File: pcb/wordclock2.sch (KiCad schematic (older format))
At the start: 3 parts

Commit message: progress
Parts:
- added BT?: Battery_Cell, symbol Battery_Cell
- added C?: 100u, symbol C
- added C?: 10u, symbol C
- added C? (x3): 100n, symbol C
- added C? (x4): 22p, symbol C
- added J?: Jack-DC, symbol Jack-DC
- added J?: USB_OTG, symbol USB_OTG
- added U?: Si7021, symbol Si7021
- added U?: TPS77833_SO8, Housings_SOIC:SOIC-8_3.9x4.9mm_Pitch1.27mm, symbol TPS77833_SO8
- added Y?: 32.768kHz, symbol Crystal
- added Y?: 8MHz, symbol Crystal
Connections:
- net labels added: +3.3V, +5V, GND, USB_DM, USB_DP
- wire segments 0 -> 61
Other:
- moved on the sheet: U?

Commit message: progress
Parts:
- added BZ?: Buzzer, symbol Buzzer
- added J?: Micro_SD_Card_Det, symbol Micro_SD_Card_Det
- added J? (x2): CONN_01X03, symbol CONN_01X03
- added J?: CONN_02X05, symbol CONN_02X05
- added JP?: Jumper_NO_Small, symbol Jumper_NO_Small
- added R? (x3): 4k7, symbol R
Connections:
- net labels added: BOOT0, ST_NRST, SWCLK, SWDIO, SWO, UART_DBG_RX, UART_DBG_TX, UART_WLAN_RX, UART_WLAN_TX
- wire segments 61 -> 101

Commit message: progress
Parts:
- added Q? (x2): FDS6890A, Housings_SOIC:SOIC-8_3.9x4.9mm_Pitch1.27mm, symbol FDS6890A
- added SW?: SW_Push, symbol SW_Push
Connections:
- wire segments 101 -> 116
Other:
- moved on the sheet: BZ?, J?
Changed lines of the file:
@@
 encoding utf-8
 Sheet 1 1
-Title ""
+Title "Wordclock2"
 Date ""
 Rev ""
@@
 L Micro_SD_Card_Det J?
 U 1 1 5983AA78
-P 5150 6750
-F 0 "J?" H 4500 7450 50  0000 C CNN
-F 1 "Micro_SD_Card_Det" H 5800 7450 50  0000 R CNN
-F 2 "" H 7200 7450 50  0001 C CNN
-F 3 "" H 5150 6850 50  0001 C CNN
-	1    5150 6750
+P 5150 6500
+F 0 "J?" H 4500 7200 50  0000 C CNN
+F 1 "Micro_SD_Card_Det" H 5800 7200 50  0000 R CNN
+F 2 "" H 7200 7200 50  0001 C CNN
+F 3 "" H 5150 6600 50  0001 C CNN
+	1    5150 6500
 	1    0    0    -1
 $EndComp
@@
 L Buzzer BZ?
 U 1 1 5983AD21
-P 3800 5450
-F 0 "BZ?" H 3950 5500 50  0000 L CNN
-F 1 "Buzzer" H 3950 5400 50  0000 L CNN
-F 2 "" V 3775 5550 50  0001 C CNN
-F 3 "" V 3775 5550 50  0001 C CNN
-	1    3800 5450
+P 3750 5100
+F 0 "BZ?" H 3900 5150 50  0000 L CNN
+F 1 "Buzzer" H 3900 5050 50  0000 L CNN
+F 2 "" V 3725 5200 50  0001 C CNN
+F 3 "" V 3725 5200 50  0001 C CNN
+	1    3750 5100
 	1    0    0    -1
 $EndComp
@@
 	4600 700  4600 650
 Wire Wire Line
-	5150 900  5550 900
-Text Label 5200 900  0    60   ~ 0
+	5150 900  5800 900
+Text Label 5200 800  0    60   ~ 0
 BOOT0
 Wire Wire Line
@@
 Wire Wire Line
 	5150 800  5800 800
-Text Label 5150 800  0    60   ~ 0
+Text Label 5200 900  0    60   ~ 0
 UART_DBG_RX
 $Comp
@@
 Wire Wire Line
 	5900 1200 5900 1150
+$Comp
+L SW_Push SW?
+U 1 1 5984DFFE
+P 1300 3100
+F 0 "SW?" H 1350 3200 50  0000 L CNN
+F 1 "SW_Push" H 1300 3040 50  0000 C CNN
+F 2 "" H 1300 3300 50  0001 C CNN
+F 3 "" H 1300 3300 50  0001 C CNN
+	1    1300 3100
+	1    0    0    -1
+$EndComp
+$Comp
+L GND #PWR?
+U 1 1 5984E29E
+P 1050 3150
+F 0 "#PWR?" H 1050 2900 50  0001 C CNN
+F 1 "GND" H 1050 3000 50  0000 C CNN
+F 2 "" H 1050 3150 50  0001 C CNN
+F 3 "" H 1050 3150 50  0001 C CNN
+	1    1050 3150
+	1    0    0    -1
+$EndComp
+Wire Wire Line
+	1100 3100 1050 3100
+Wire Wire Line
+	1050 3100 1050 3150
+Wire Wire Line
+	1500 3100 1950 3100
+Text Label 1550 3100 0    60   ~ 0
+ST_NRST
+$Comp
+L FDS6890A Q?
+U 1 1 5984ED73
+P 3700 7300
+F 0 "Q?" H 3950 7375 50  0000 L CNN
+F 1 "FDS6890A" H 3950 7300 50  0000 L CNN
+F 2 "Housings_SOIC:SOIC-8_3.9x4.9mm_Pitch1.27mm" H 3950 7225 50  0001 L CIN
+F 3 "" H 3700 7300 50  0001 L CNN
+	1    3700 7300
+	1    0    0    -1
+$EndComp
+$Comp
+L FDS6890A Q?
+U 2 1 5984F828
+P 3450 5500
+F 0 "Q?" H 3700 5575 50  0000 L CNN
+F 1 "FDS6890A" H 3700 5500 50  0000 L CNN
+F 2 "Housings_SOIC:SOIC-8_3.9x4.9mm_Pitch1.27mm" H 3700 5425 50  0001 L CIN
+F 3 "" H 3450 5500 50  0001 L CNN
+	2    3450 5500
+	1    0    0    -1
+$EndComp
+Wire Wire Line
+	3650 5200 3550 5200
+Wire Wire Line
+	3550 5200 3550 5300
+Wire Wire Line
+	3650 5200 3650 5300
+Wire Wire Line
+	3550 5700 3550 5750
+$Comp
+L GND #PWR?
+U 1 1 59850461
+P 3550 5750
+F 0 "#PWR?" H 3550 5500 50  0001 C CNN
+F 1 "GND" H 3550 5600 50  0000 C CNN
+F 2 "" H 3550 5750 50  0001 C CNN
+F 3 "" H 3550 5750 50  0001 C CNN
+	1    3550 5750
+	1    0    0    -1
+$EndComp
+$Comp
+L +3.3V #PWR?
+U 1 1 59850E3B
+P 3650 4950
+F 0 "#PWR?" H 3650 4800 50  0001 C CNN
+F 1 "+3.3V" H 3650 5090 50  0000 C CNN
+F 2 "" H 3650 4950 50  0001 C CNN
+F 3 "" H 3650 4950 50  0001 C CNN
+	1    3650 4950
+	1    0    0    -1
+$EndComp
+Wire Wire Line
+	3650 4950 3650 5000
+Wire Wire Line
+	4250 6600 3800 6600
+Wire Wire Line
+	3800 6600 3800 7100
+Wire Wire Line
+	3800 7050 3900 7050
+Wire Wire Line
+	3900 7050 3900 7100
+Connection ~ 3800 7050
+$Comp
+L GND #PWR?
+U 1 1 598518E3
+P 3800 7550
+F 0 "#PWR?" H 3800 7300 50  0001 C CNN
+F 1 "GND" H 3800 7400 50  0000 C CNN
+F 2 "" H 3800 7550 50  0001 C CNN
+F 3 "" H 3800 7550 50  0001 C CNN
+	1    3800 7550
+	1    0    0    -1
+$EndComp
+Wire Wire Line
+	3800 7500 3800 7550
+$Comp
+L +3.3V #PWR?
+U 1 1 59852472
+P 4000 6000
+F 0 "#PWR?" H 4000 5850 50  0001 C CNN
+F 1 "+3.3V" H 4000 6140 50  0000 C CNN
+F 2 "" H 4000 6000 50  0001 C CNN
+F 3 "" H 4000 6000 50  0001 C CNN
+	1    4000 6000
+	1    0    0    -1
+$EndComp
+Wire Wire Line
+	4250 6400 4000 6400
+Wire Wire Line
+	4000 6400 4000 6000
 $EndSCHEMATC

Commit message: progress
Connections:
- net labels added: BUZZ_EN, I2C_SCL, I2C_SDA, LEDStripe1, LEDStripe2, SD_CS, SD_DET, SD_EN, SPI_MISO, SPI_MOSI, SPI_SCK
- wire segments 116 -> 149
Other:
- moved on the sheet: U?
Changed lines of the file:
@@
 L MAXIM_MAX44009 U?
 U 1 1 598237BF
-P 2400 6600
-F 0 "U?" H 2400 6900 60  0000 C CNN
-F 1 "MAXIM_MAX44009" H 2400 6300 60  0000 C CNN
-F 2 "" H 2500 6500 60  0000 C CNN
-F 3 "" H 2500 6500 60  0000 C CNN
-	1    2400 6600
+P 1750 6600
+F 0 "U?" H 1750 6900 60  0000 C CNN
+F 1 "MAXIM_MAX44009" H 1750 6300 60  0000 C CNN
+F 2 "" H 1850 6500 60  0000 C CNN
+F 3 "" H 1850 6500 60  0000 C CNN
+	1    1750 6600
 	1    0    0    -1
 $EndComp
@@
 L Si7021 U?
 U 1 1 5982FE83
-P 2400 4950
-F 0 "U?" H 2300 5150 60  0000 C CNN
-F 1 "Si7021" H 2650 4700 60  0000 C CNN
-F 2 "" H 2450 4750 60  0000 C CNN
-F 3 "" H 2450 4750 60  0000 C CNN
-	1    2400 4950
+P 1900 4850
+F 0 "U?" H 1800 5050 60  0000 C CNN
+F 1 "Si7021" H 2150 4600 60  0000 C CNN
+F 2 "" H 1950 4650 60  0000 C CNN
+F 3 "" H 1950 4650 60  0000 C CNN
+	1    1900 4850
 	1    0    0    -1
 $EndComp
@@
 $EndComp
 Wire Wire Line
-	7350 3550 7950 3550
-Wire Wire Line
-	7350 3450 7950 3450
+	7350 3550 8050 3550
+Wire Wire Line
+	7350 3450 8050 3450
 Text Label 7400 3550 0    60   ~ 0
 USB_DP
@@
 	3650 4950 3650 5000
 Wire Wire Line
-	4250 6600 3800 6600
-Wire Wire Line
-	3800 6600 3800 7100
-Wire Wire Line
-	3800 7050 3900 7050
+	3800 7050 4000 7050
 Wire Wire Line
 	3900 7050 3900 7100
-Connection ~ 3800 7050
 $Comp
 L GND #PWR?
@@
 Wire Wire Line
 	4000 6400 4000 6000
+Wire Wire Line
+	4250 6200 3500 6200
+Text Label 3550 6200 0    60   ~ 0
+SD_CS
+Wire Wire Line
+	4250 6300 3500 6300
+Text Label 3550 6300 0    60   ~ 0
+SPI_MOSI
+Wire Wire Line
+	4250 6500 3500 6500
+Wire Wire Line
+	4250 6700 3500 6700
+Wire Wire Line
+	4250 6600 4000 6600
+Wire Wire Line
+	4000 6600 4000 7050
+Connection ~ 3900 7050
+Wire Wire Line
+	3800 7050 3800 7100
+Text Label 3550 6500 0    60   ~ 0
+SPI_SCK
+Text Label 3550 6700 0    60   ~ 0
+SPI_MISO
+Wire Wire Line
+	7350 2350 8050 2350
+Wire Wire Line
+	7350 2450 8050 2450
+Text Label 7400 2350 0    60   ~ 0
+LEDStripe1
+Text Label 7400 2450 0    60   ~ 0
+LEDStripe2
+Wire Wire Line
+	9900 1650 10600 1650
+Wire Wire Line
+	9900 2450 10600 2450
+Text Label 9950 1650 0    60   ~ 0
+LEDStripe1
+Text Label 9950 2450 0    60   ~ 0
+LEDStripe2
+Text Label 7400 2750 0    60   ~ 0
+SD_CS
+Text Label 7400 3050 0    60   ~ 0
+SPI_MOSI
+Text Label 7400 2850 0    60   ~ 0
+SPI_SCK
+Text Label 7400 2950 0    60   ~ 0
+SPI_MISO
+Wire Wire Line
+	7350 2750 8050 2750
+Wire Wire Line
+	7350 2850 8050 2850
+Wire Wire Line
+	7350 2950 8050 2950
+Wire Wire Line
+	7350 3050 8050 3050
+Text Label 2800 5550 0    60   ~ 0
+BUZZ_EN
+Wire Wire Line
+	3250 5550 2800 5550
+Text Label 3200 7350 0    60   ~ 0
+SD_EN
+Wire Wire Line
+	3500 7350 3200 7350
+Wire Wire Line
+	7350 3900 8050 3900
+Text Label 7400 3900 0    60   ~ 0
+SD_EN
+Wire Wire Line
+	7350 4000 8050 4000
+Text Label 7400 4000 0    60   ~ 0
+BUZZ_EN
+Wire Wire Line
+	4250 6900 3500 6900
+$Comp
+L GND #PWR?
+U 1 1 5985FEFF
+P 4200 7050
+F 0 "#PWR?" H 4200 6800 50  0001 C CNN
+F 1 "GND" H 4200 6900 50  0000 C CNN
+F 2 "" H 4200 7050 50  0001 C CNN
+F 3 "" H 4200 7050 50  0001 C CNN
+	1    4200 7050
+	1    0    0    -1
+$EndComp
+Wire Wire Line
+	4250 7000 4200 7000
+Wire Wire Line
+	4200 7000 4200 7050
+Text Label 3550 6900 0    60   ~ 0
+SD_DET
+Wire Wire Line
+	7350 4100 8050 4100
+Text Label 7400 4100 0    60   ~ 0
+SD_DET
+Wire Wire Line
+	5100 4250 4450 4250
+Wire Wire Line
+	5100 4350 4450 4350
+Text Label 4500 4250 0    60   ~ 0
+I2C_SDA
+Text Label 4500 4350 0    60   ~ 0
+I2C_SCL
+$Comp
+L +3.3V #PWR?
+U 1 1 598615CD
+P 1950 4500
+F 0 "#PWR?" H 1950 4350 50  0001 C CNN
+F 1 "+3.3V" H 1950 4640 50  0000 C CNN
+F 2 "" H 1950 4500 50  0001 C CNN
+F 3 "" H 1950 4500 50  0001 C CNN
+	1    1950 4500
+	1    0    0    -1
+$EndComp
+$Comp
+L GND #PWR?
+U 1 1 598616B1
+P 1950 5250
+F 0 "#PWR?" H 1950 5000 50  0001 C CNN
+F 1 "GND" H 1950 5100 50  0000 C CNN
+F 2 "" H 1950 5250 50  0001 C CNN
+F 3 "" H 1950 5250 50  0001 C CNN
+	1    1950 5250
+	1    0    0    -1
+$EndComp
+Wire Wire Line
+	1950 4500 1950 4550
+Wire Wire Line
+	1950 5200 1950 5250
+Wire Wire Line
+	1600 4800 950  4800
+Wire Wire Line
+	1600 4950 950  4950
+Text Label 1000 4800 0    60   ~ 0
+I2C_SDA
+Text Label 1000 4950 0    60   ~ 0
+I2C_SCL
+Text Label 2350 6500 0    60   ~ 0
+I2C_SDA
+Text Label 2350 6600 0    60   ~ 0
+I2C_SCL
+Wire Wire Line
+	2300 6500 2750 6500
+Wire Wire Line
+	2300 6600 2750 6600
+$Comp
+L +3.3V #PWR?
+U 1 1 598627C3
+P 1150 6450
+F 0 "#PWR?" H 1150 6300 50  0001 C CNN
+F 1 "+3.3V" H 1150 6590 50  0000 C CNN
+F 2 "" H 1150 6450 50  0001 C CNN
+F 3 "" H 1150 6450 50  0001 C CNN
+	1    1150 6450
+	1    0    0    -1
+$EndComp
+Wire Wire Line
+	1200 6500 1150 6500
+Wire Wire Line
+	1150 6500 1150 6450
+$Comp
+L GND #PWR?
+U 1 1 5986296F
+P 1150 6750
+F 0 "#PWR?" H 1150 6500 50  0001 C CNN
+F 1 "GND" H 1150 6600 50  0000 C CNN
+F 2 "" H 1150 6750 50  0001 C CNN
+F 3 "" H 1150 6750 50  0001 C CNN
+	1    1150 6750
+	1    0    0    -1
+$EndComp
+Wire Wire Line
+	1200 6600 1150 6600
+Wire Wire Line
+	1150 6600 1150 6750
 $EndSCHEMATC

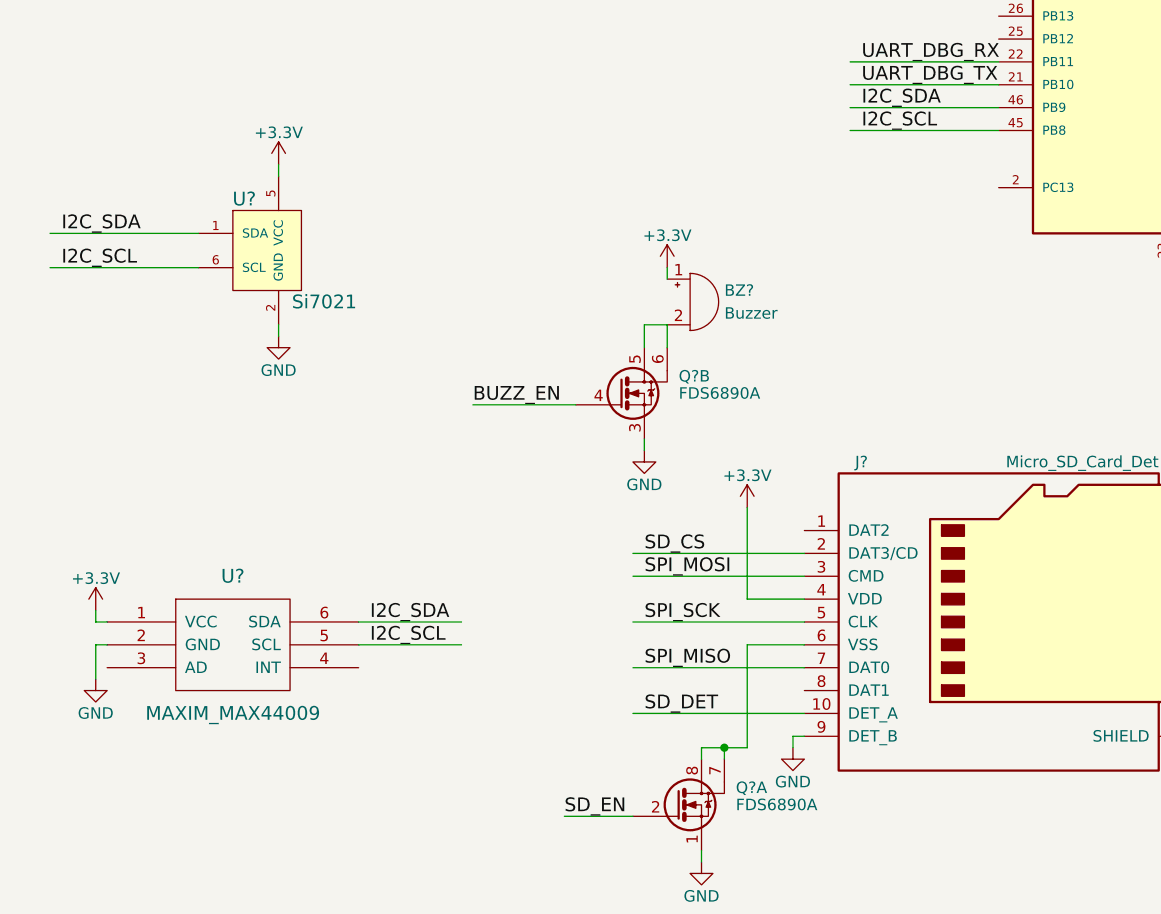
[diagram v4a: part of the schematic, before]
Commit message: added datasheets
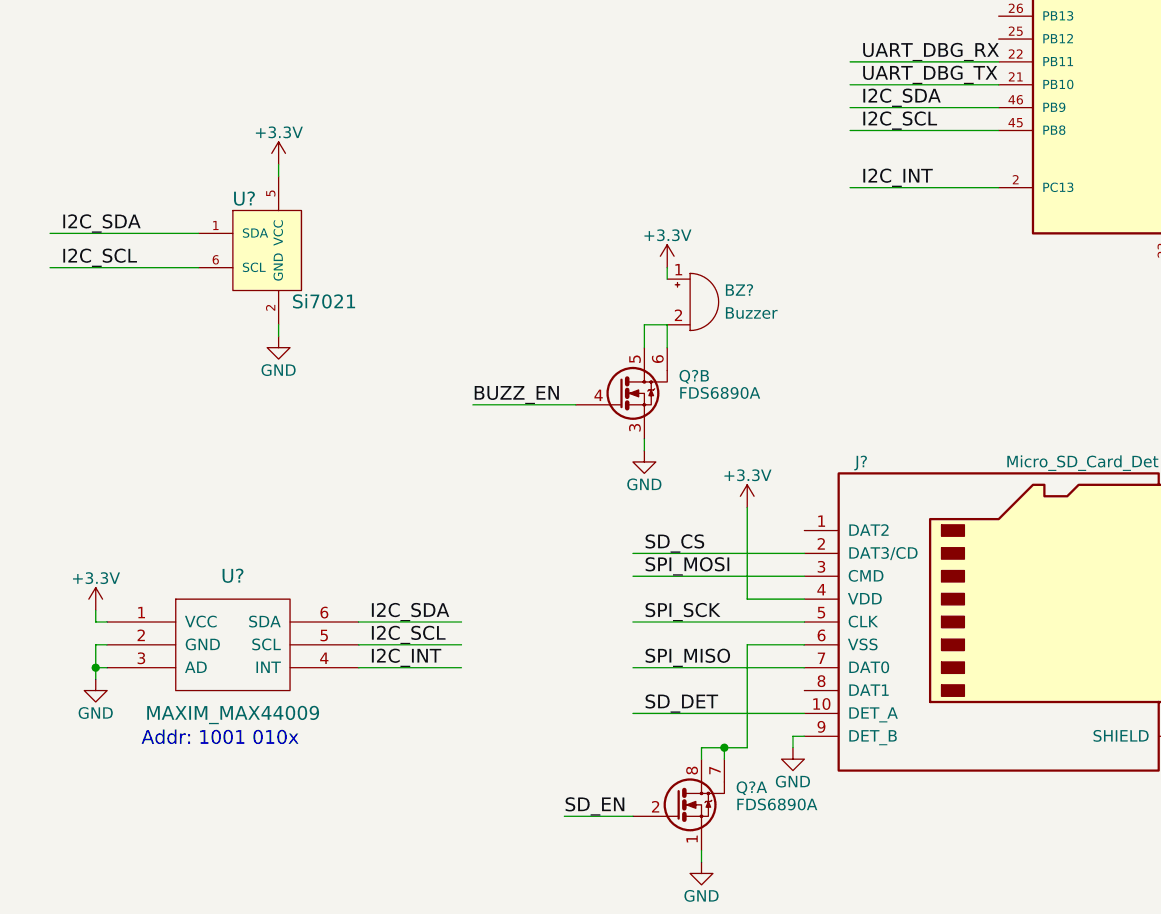
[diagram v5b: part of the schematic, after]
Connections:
- net labels added: I2C_INT
- wire segments 149 -> 152
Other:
- note added: "Addr: 1001 010x"
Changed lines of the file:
@@
 Wire Wire Line
 	1150 6600 1150 6750
+Wire Wire Line
+	1200 6700 1150 6700
+Connection ~ 1150 6700
+Text Notes 1350 7050 0    60   ~ 0
+Addr: 1001 010x
+Wire Wire Line
+	5100 4600 4450 4600
+Text Label 4500 4600 0    60   ~ 0
+I2C_INT
+Wire Wire Line
+	2300 6700 2750 6700
+Text Label 2350 6700 0    60   ~ 0
+I2C_INT
 $EndSCHEMATC

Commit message: progress
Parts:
- removed R?: 4k7, symbol R
- added C? (x2): 1u, symbol C
- added C?: 100n, symbol C
- added D? (x2): LED, symbol LED
- added R? (x2): 512, symbol R
- added R? (x3): 10k, symbol R
- added SW? (x2): SW_Push, symbol SW_Push
- R? (x2): value 4k7 -> 10k
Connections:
- net labels added: USER_BTN1, USER_BTN2, USER_LED1, USER_LED2
- wire segments 152 -> 174
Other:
- moved on the sheet: C?, U?

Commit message: progress
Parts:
- removed U?: STM32L433CCT6, LQFP48, symbol STM32L433CCT6
- added U?: STM32L433CCT6, LQFP48, symbol STM32L433CCT6
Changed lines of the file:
@@
 $EndDescr
-$Comp
-L STM32L433CCT6 U?
-U 1 1 5980B1B9
-P 6150 3450
-F 0 "U?" H 5300 4900 50  0000 L BNN
-F 1 "STM32L433CCT6" H 6600 2000 50  0000 L BNN
-F 2 "LQFP48" H 6200 3450 50  0001 C CIN
-F 3 "" H 6400 3350 50  0001 C CNN
-	1    6150 3450
-	1    0    0    -1
-$EndComp
 $Comp
 L ESP-12E U?
@@
 	3850 4600 4150 4600
 Connection ~ 3850 4350
+$Comp
+L STM32L433CCT6 U?
+U 1 1 59872B3C
+P 6150 3450
+F 0 "U?" H 5300 4900 50  0000 L BNN
+F 1 "STM32L433CCT6" H 6600 2000 50  0000 L BNN
+F 2 "LQFP48" H 6200 3450 50  0001 C CIN
+F 3 "" H 6400 3350 50  0001 C CNN
+	1    6150 3450
+	1    0    0    -1
+$EndComp
 $EndSCHEMATC

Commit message: progress
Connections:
- net labels added: UART_OTA_RX, UART_OTA_TX
- wire segments 174 -> 178
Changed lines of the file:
@@
 	1    0    0    -1
 $EndComp
+Wire Wire Line
+	7350 3250 8050 3250
+Wire Wire Line
+	7350 3350 8050 3350
+Text Label 7400 3250 0    60   ~ 0
+UART_OTA_TX
+Text Label 7400 3350 0    60   ~ 0
+UART_OTA_RX
+Wire Wire Line
+	9800 5250 10500 5250
+Wire Wire Line
+	7300 5250 8000 5250
+Text Label 9850 5250 0    60   ~ 0
+UART_OTA_TX
+Text Label 7350 5250 0    60   ~ 0
+UART_OTA_RX
 $EndSCHEMATC
